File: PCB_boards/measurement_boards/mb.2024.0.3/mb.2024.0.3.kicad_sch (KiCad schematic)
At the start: 27 parts, among them J1 DPS_out_12v_GND, J10 DPS+, J11 Screw_Terminal_VMN, J13 Connector_I2C_for_mux, J16 RX_bat, J17 DPS GND, J18 ELEC_M, J19 ELEC_N, J2 DPS5005_input_0_to_50V, J22 Conn_01x04_Socket, J23 Conn_01x05_Socket, J24 Connector_I2C_for_MC, J25 Conn_01x04_Socket, J26 Conn_01x05_Socket, J3 Screw_Terminal_AB, J4 Conn_01x08_Socket, J5 Conn_01x04_Socket, J6 Conn_01x08_Socket, J7 Raspberry_Pi_2_3, J8 Connector_I2C_for_MCP23008, J9 TX_bat, U1 MCP23008-xP, U3 24LC02

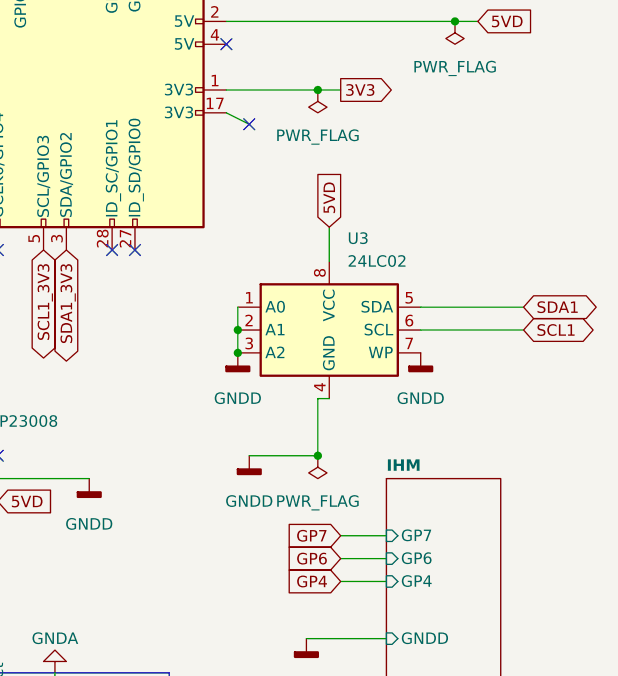
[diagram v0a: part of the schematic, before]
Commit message: last version of mesaurement board correction of web site adresse, named i2C EXT, I2C MUX and I2C Vmn, delete unused components
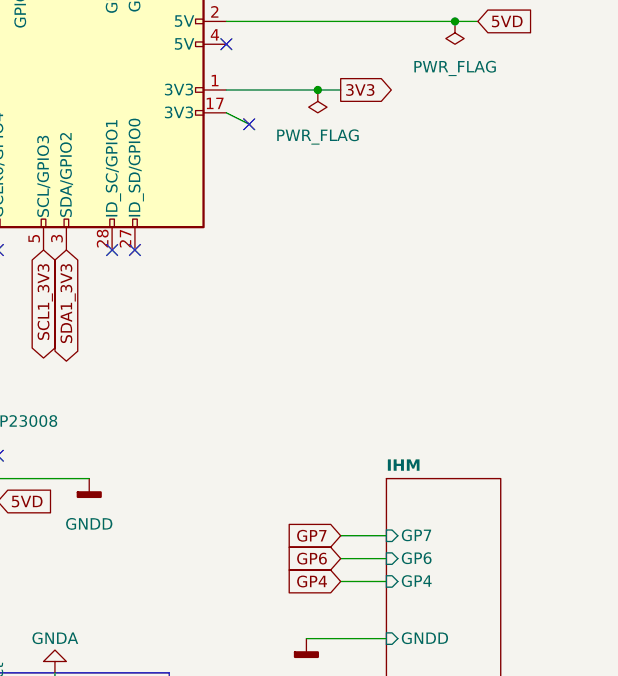
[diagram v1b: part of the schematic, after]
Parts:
- removed U3: 24LC02, Package_DIP:DIP-8_W7.62mm, symbol Memory_EEPROM:24LC02
